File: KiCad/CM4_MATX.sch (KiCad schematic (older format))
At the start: 9 parts

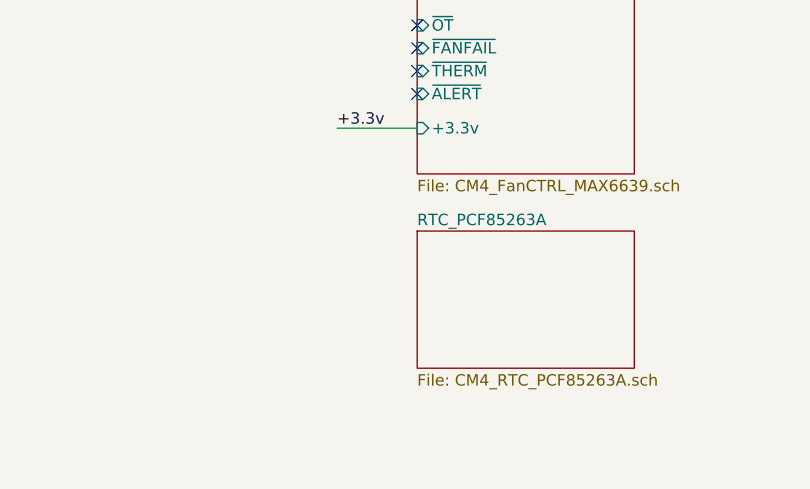
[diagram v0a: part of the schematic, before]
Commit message: updated PCB with RTC circuit
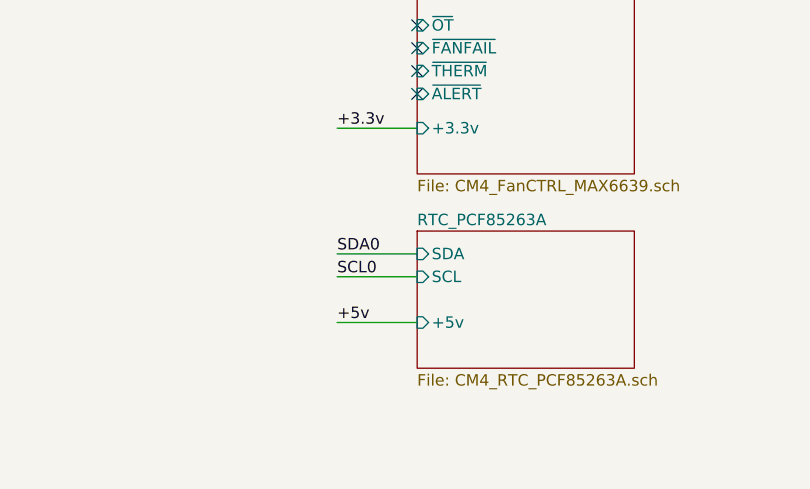
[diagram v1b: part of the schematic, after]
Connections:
- wire segments 78 -> 81
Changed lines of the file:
@@
 F0 "RTC_PCF85263A" 50
 F1 "CM4_RTC_PCF85263A.sch" 50
+F2 "SCL" I L 5400 6850 50
+F3 "SDA" I L 5400 6750 50
+F4 "+5v" I L 5400 7050 50
 $EndSheet
+Wire Wire Line
+	5050 6850 5400 6850
+Text Label 5050 6750 0    50   ~ 0
+SDA0
+Text Label 5050 6850 0    50   ~ 0
+SCL0
+Wire Wire Line
+	5400 6750 5050 6750
+Text Label 5050 7050 0    50   ~ 0
++5v
+Wire Wire Line
+	5400 7050 5050 7050
 $EndSCHEMATC

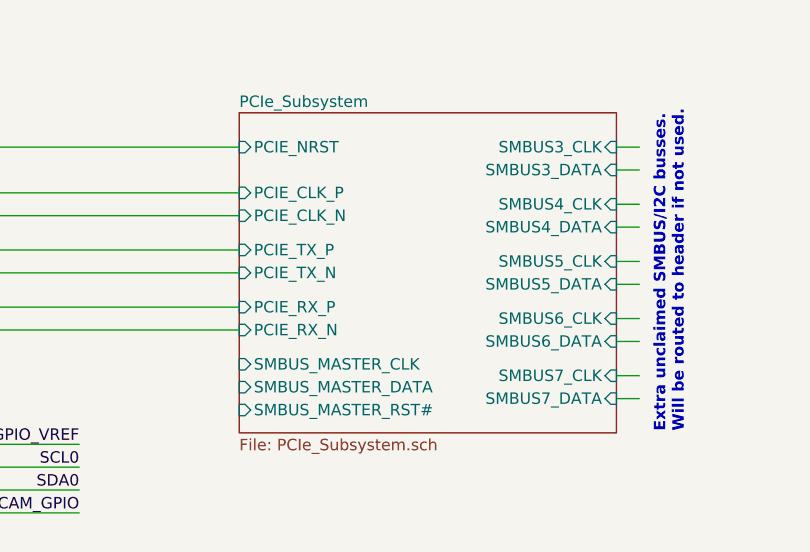
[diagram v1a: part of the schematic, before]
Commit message: Tons of wiring and pin straps for PCI-e Switch
Also re-did some hierarchical labels for JTAG
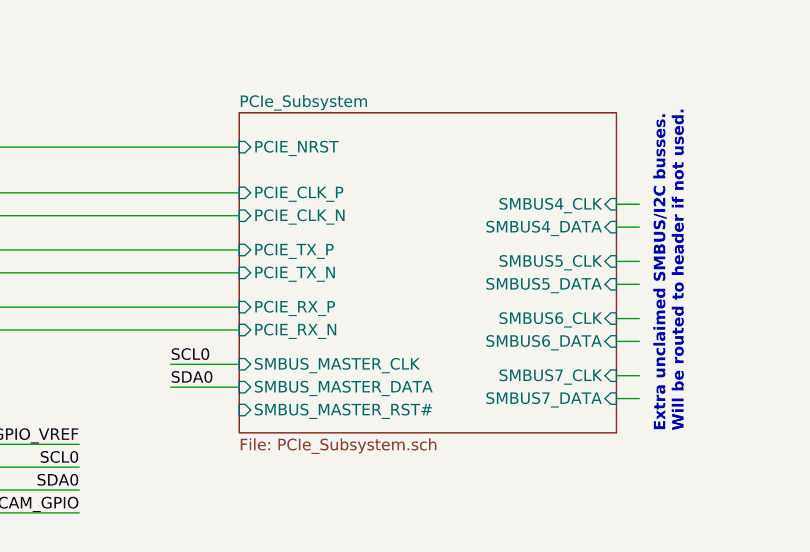
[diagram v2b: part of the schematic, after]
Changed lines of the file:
@@
 F28 "HD2_5v" I L 3050 1100 50
-$EndSheet
-$Sheet
-S 7300 1100 1650 1400
-U 5FFBC089
-F0 "PCIe_Subsystem" 50
-F1 "PCIe_Subsystem.sch" 50
-F2 "PCIE_NRST" I L 7300 1250 50
-F3 "PCIE_CLK_P" I L 7300 1450 50
-F4 "PCIE_CLK_N" I L 7300 1550 50
-F5 "PCIE_TX_P" I L 7300 1700 50
-F6 "PCIE_TX_N" I L 7300 1800 50
-F7 "PCIE_RX_P" I L 7300 1950 50
-F8 "PCIE_RX_N" I L 7300 2050 50
-F9 "SMBUS3_CLK" I R 8950 1250 50
-F10 "SMBUS3_DATA" I R 8950 1350 50
-F11 "SMBUS4_CLK" I R 8950 1500 50
-F12 "SMBUS4_DATA" I R 8950 1600 50
-F13 "SMBUS5_CLK" I R 8950 1750 50
-F14 "SMBUS5_DATA" I R 8950 1850 50
-F15 "SMBUS6_CLK" I R 8950 2000 50
-F16 "SMBUS6_DATA" I R 8950 2100 50
-F17 "SMBUS7_CLK" I R 8950 2250 50
-F18 "SMBUS7_DATA" I R 8950 2350 50
-F19 "SMBUS_MASTER_CLK" I L 7300 2200 50
-F20 "SMBUS_MASTER_DATA" I L 7300 2300 50
-F21 "SMBUS_MASTER_RST#" I L 7300 2400 50
 $EndSheet
 Wire Wire Line
@@
 Wire Wire Line
 	6150 2050 7300 2050
-Wire Wire Line
-	8950 1250 9050 1250
-Wire Wire Line
-	8950 1350 9050 1350
 Wire Wire Line
 	8950 1500 9050 1500
@@
 Wire Wire Line
 	5400 7050 5050 7050
+Text Label 7000 2200 0    50   ~ 0
+SCL0
+Text Label 7000 2300 0    50   ~ 0
+SDA0
+Wire Wire Line
+	7000 2200 7300 2200
+Wire Wire Line
+	7300 2300 7000 2300
+$Sheet
+S 7300 1100 1650 1400
+U 5FFBC089
+F0 "PCIe_Subsystem" 50
+F1 "PCIe_Subsystem.sch" 50
+F2 "PCIE_NRST" I L 7300 1250 50
+F3 "PCIE_CLK_P" I L 7300 1450 50
+F4 "PCIE_CLK_N" I L 7300 1550 50
+F5 "PCIE_TX_P" I L 7300 1700 50
+F6 "PCIE_TX_N" I L 7300 1800 50
+F7 "PCIE_RX_P" I L 7300 1950 50
+F8 "PCIE_RX_N" I L 7300 2050 50
+F9 "SMBUS4_CLK" I R 8950 1500 50
+F10 "SMBUS4_DATA" I R 8950 1600 50
+F11 "SMBUS5_CLK" I R 8950 1750 50
+F12 "SMBUS5_DATA" I R 8950 1850 50
+F13 "SMBUS6_CLK" I R 8950 2000 50
+F14 "SMBUS6_DATA" I R 8950 2100 50
+F15 "SMBUS7_CLK" I R 8950 2250 50
+F16 "SMBUS7_DATA" I R 8950 2350 50
+F17 "SMBUS_MASTER_CLK" I L 7300 2200 50
+F18 "SMBUS_MASTER_DATA" I L 7300 2300 50
+F19 "SMBUS_MASTER_RST#" I L 7300 2400 50
+$EndSheet
 $EndSCHEMATC

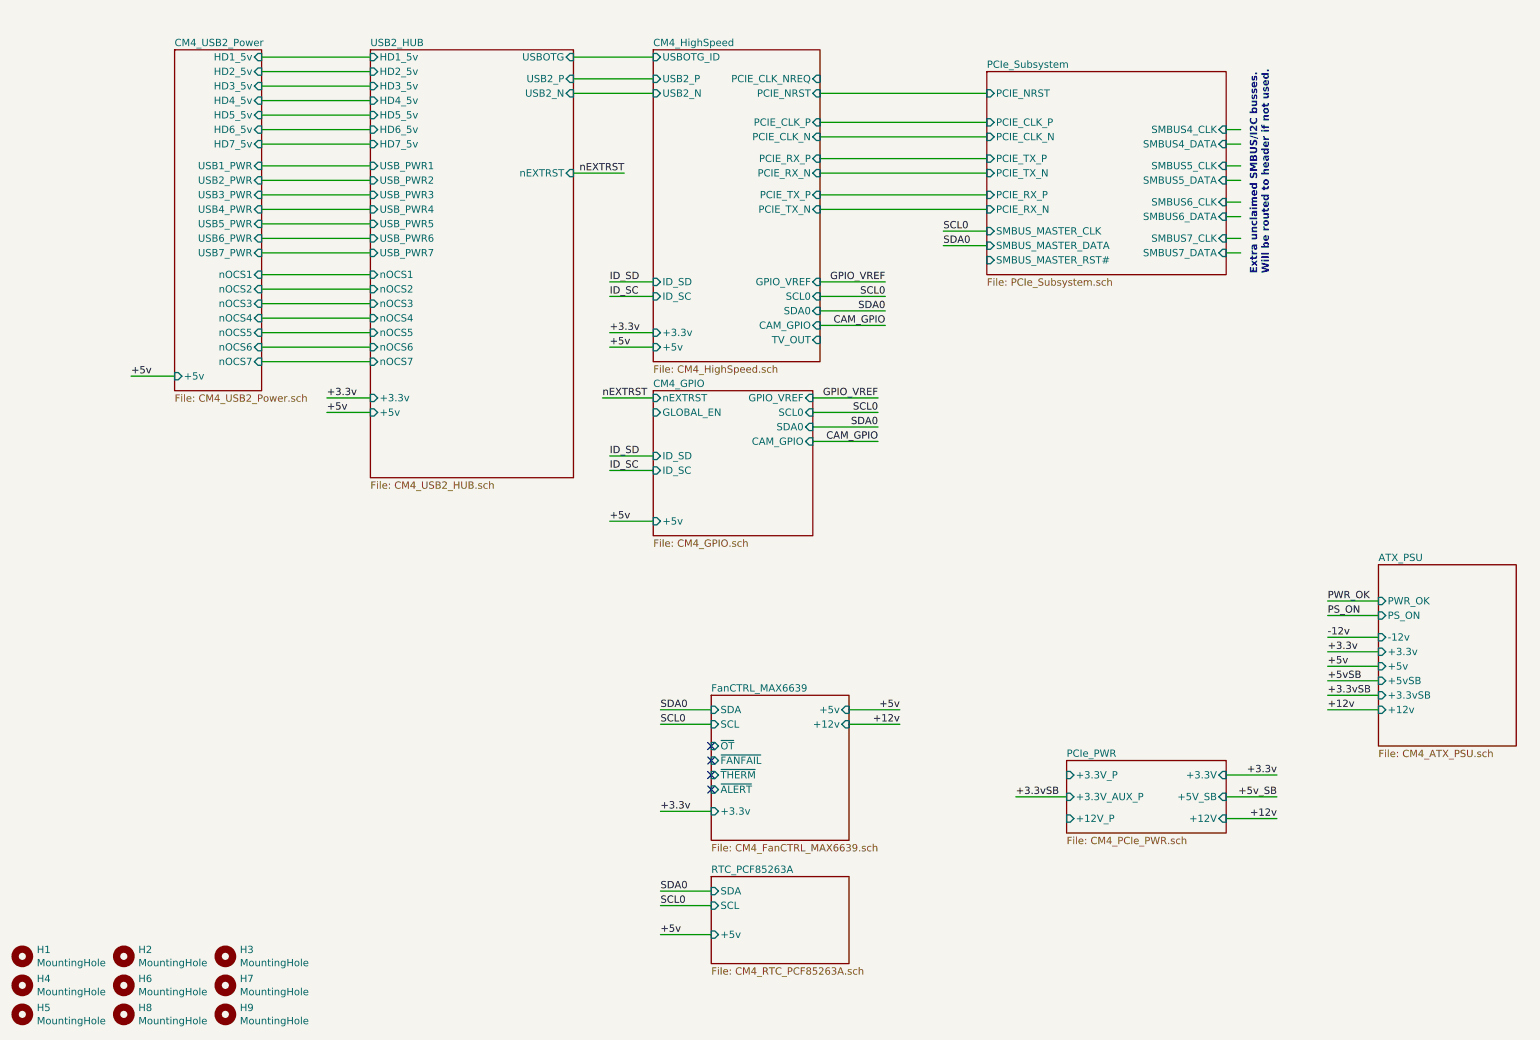
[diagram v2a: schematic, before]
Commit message: PCIe Wiring, resistor value adjustments, and a bunch of small ERC fixes.
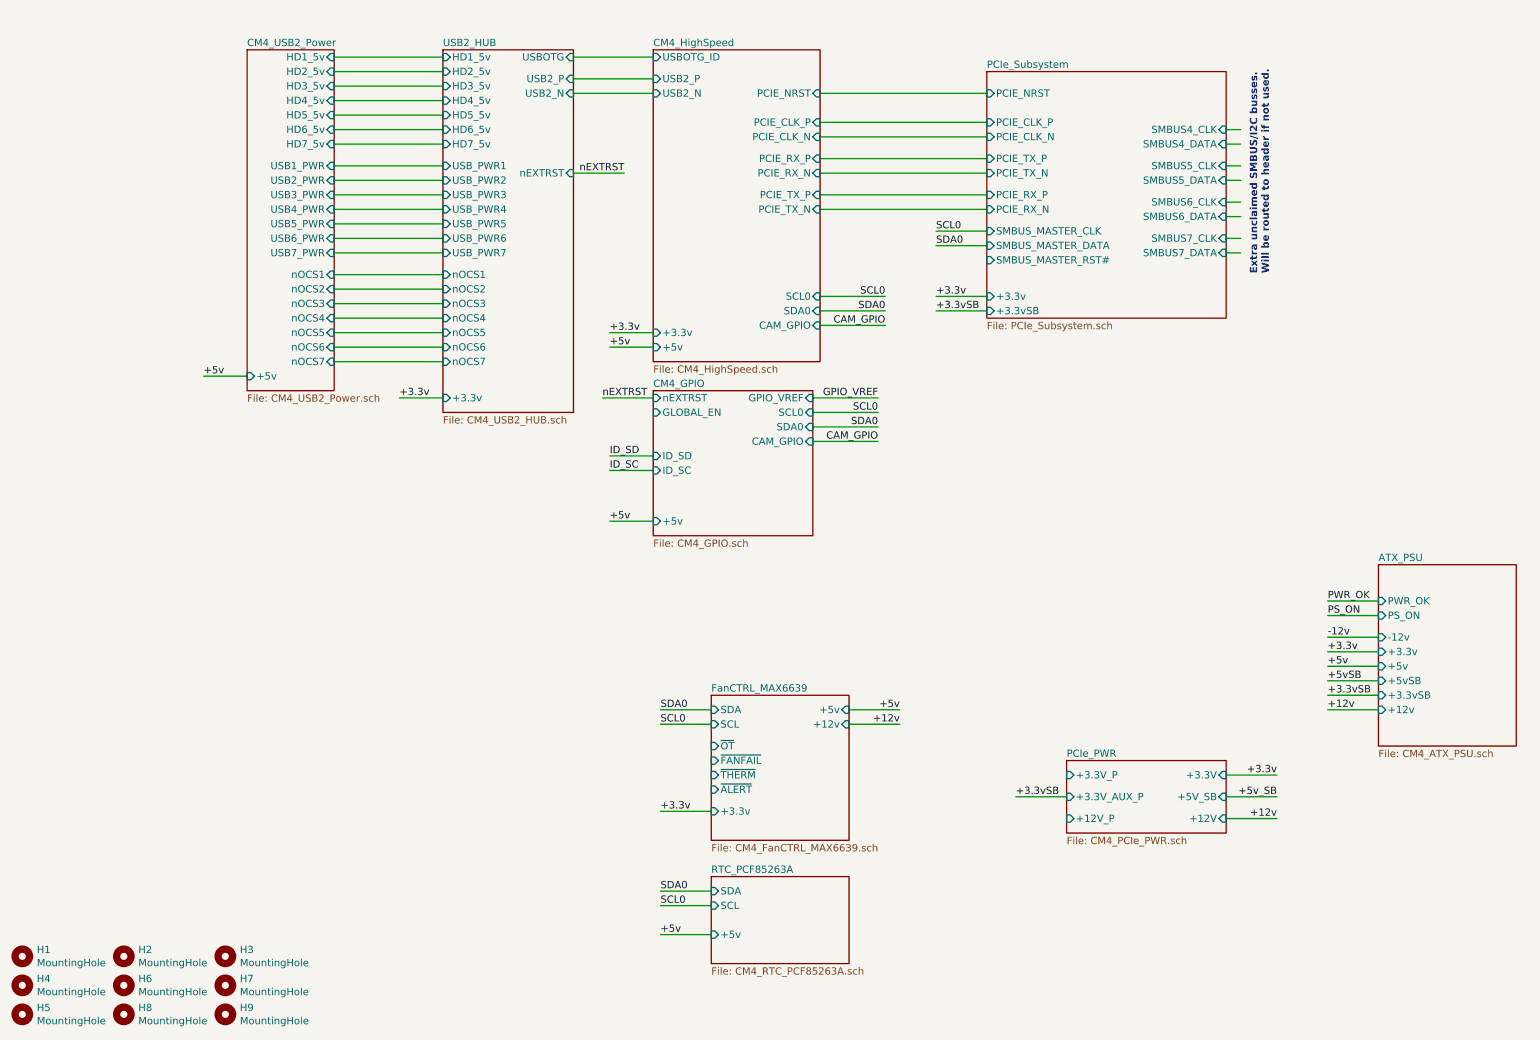
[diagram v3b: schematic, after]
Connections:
- wire segments 81 -> 79
- no-connect marks 4 -> 0
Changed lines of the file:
@@
 F0 "CM4_HighSpeed" 50
 F1 "CM4_HighSpeed.sch" 50
-F2 "TV_OUT" I R 6150 2950 50
-F3 "PCIE_NRST" I R 6150 1250 50
-F4 "USB2_P" I L 5000 1150 50
-F5 "USB2_N" I L 5000 1250 50
-F6 "USBOTG_ID" I L 5000 1000 50
-F7 "CAM_GPIO" I R 6150 2850 50
-F8 "PCIE_CLK_NREQ" I R 6150 1150 50
-F9 "PCIE_CLK_P" I R 6150 1450 50
-F10 "PCIE_CLK_N" I R 6150 1550 50
-F11 "PCIE_RX_P" I R 6150 1700 50
-F12 "PCIE_RX_N" I R 6150 1800 50
-F13 "PCIE_TX_P" I R 6150 1950 50
-F14 "PCIE_TX_N" I R 6150 2050 50
-F15 "+3.3v" I L 5000 2900 50
-F16 "SDA0" I R 6150 2750 50
-F17 "SCL0" I R 6150 2650 50
-F18 "GPIO_VREF" I R 6150 2550 50
-F19 "ID_SC" I L 5000 2650 50
-F20 "ID_SD" I L 5000 2550 50
-F21 "+5v" I L 5000 3000 50
+F2 "PCIE_NRST" I R 6150 1250 50
+F3 "USB2_P" I L 5000 1150 50
+F4 "USB2_N" I L 5000 1250 50
+F5 "USBOTG_ID" I L 5000 1000 50
+F6 "CAM_GPIO" I R 6150 2850 50
+F7 "PCIE_CLK_P" I R 6150 1450 50
+F8 "PCIE_CLK_N" I R 6150 1550 50
+F9 "PCIE_RX_P" I R 6150 1700 50
+F10 "PCIE_RX_N" I R 6150 1800 50
+F11 "PCIE_TX_P" I R 6150 1950 50
+F12 "PCIE_TX_N" I R 6150 2050 50
+F13 "+3.3v" I L 5000 2900 50
+F14 "SDA0" I R 6150 2750 50
+F15 "SCL0" I R 6150 2650 50
+F16 "+5v" I L 5000 3000 50
 $EndSheet
 $Sheet
@@
 +5v
 Wire Wire Line
-	5000 2550 4700 2550
-Text Label 4700 2550 0    50   ~ 0
-ID_SD
-Text Label 4700 2650 0    50   ~ 0
-ID_SC
-Wire Wire Line
-	4700 2650 5000 2650
-Wire Wire Line
 	5000 3750 4700 3750
 Text Label 4700 3750 0    50   ~ 0
@@
 	4450 1000 5000 1000
 Text Label 6550 3350 2    50   ~ 0
-GPIO_VREF
-Text Label 6600 2550 2    50   ~ 0
 GPIO_VREF
 Text Label 6600 2650 2    50   ~ 0
@@
 Wire Wire Line
 	6600 2650 6150 2650
-Wire Wire Line
-	6150 2550 6600 2550
 $Sheet
 S 5000 3300 1100 1000
@@
 Wire Wire Line
 	5400 5500 5050 5500
-NoConn ~ 5400 5750
-NoConn ~ 5400 5850
-NoConn ~ 5400 5950
-NoConn ~ 5400 6050
 Text Label 9650 5400 0    50   ~ 0
 +3.3vSB
@@
 	7500 6100 7850 6100
 Wire Wire Line
-	2300 1850 3050 1850
-Wire Wire Line
-	2300 1950 3050 1950
-Wire Wire Line
-	2300 2050 3050 2050
-Wire Wire Line
-	2300 2150 3050 2150
-Wire Wire Line
-	2300 2250 3050 2250
-Wire Wire Line
-	2300 2350 3050 2350
-Wire Wire Line
-	2300 1750 3050 1750
-Wire Wire Line
-	2300 1600 3050 1600
-Wire Wire Line
-	2300 1500 3050 1500
-Wire Wire Line
-	2300 1400 3050 1400
-Wire Wire Line
-	2300 1300 3050 1300
-Wire Wire Line
-	2300 1200 3050 1200
-Wire Wire Line
-	2300 1100 3050 1100
-Wire Wire Line
-	2300 1000 3050 1000
-Wire Wire Line
-	2300 2500 3050 2500
-Wire Wire Line
-	2300 2600 3050 2600
-Wire Wire Line
-	2300 2700 3050 2700
-Wire Wire Line
-	2300 2800 3050 2800
-Wire Wire Line
-	2300 2900 3050 2900
-Wire Wire Line
-	2300 3000 3050 3000
-Wire Wire Line
-	2300 3100 3050 3100
-$Sheet
-S 1700 950  600  2350
+	2800 1850 3550 1850
+Wire Wire Line
+	2800 1950 3550 1950
+Wire Wire Line
+	2800 2050 3550 2050
+Wire Wire Line
+	2800 2150 3550 2150
+Wire Wire Line
+	2800 2250 3550 2250
+Wire Wire Line
+	2800 2350 3550 2350
+Wire Wire Line
+	2800 1750 3550 1750
+Wire Wire Line
+	2800 1600 3550 1600
+Wire Wire Line
+	2800 1500 3550 1500
+Wire Wire Line
+	2800 1400 3550 1400
+Wire Wire Line
+	2800 1300 3550 1300
+Wire Wire Line
+	2800 1200 3550 1200
+Wire Wire Line
+	2800 1100 3550 1100
+Wire Wire Line
+	2800 1000 3550 1000
+Wire Wire Line
+	2800 2500 3550 2500
+Wire Wire Line
+	2800 2600 3550 2600
+Wire Wire Line
+	2800 2700 3550 2700
+Wire Wire Line
+	2800 2800 3550 2800
+Wire Wire Line
+	2800 2900 3550 2900
+Wire Wire Line
+	2800 3000 3550 3000
+Wire Wire Line
+	2800 3100 3550 3100
+$Sheet
+S 2200 950  600  2350
 U 608D2490
 F0 "CM4_USB2_Power" 50
 F1 "CM4_USB2_Power.sch" 50
-F2 "+5v" I L 1700 3200 50
-F3 "USB1_PWR" I R 2300 1750 50
-F4 "nOCS1" I R 2300 2500 50
-F5 "HD1_5v" I R 2300 1000 50
-F6 "USB2_PWR" I R 2300 1850 50
-F7 "nOCS2" I R 2300 2600 50
-F8 "HD2_5v" I R 2300 1100 50
-F9 "USB3_PWR" I R 2300 1950 50
-F10 "nOCS3" I R 2300 2700 50
-F11 "HD3_5v" I R 2300 1200 50
-F12 "USB4_PWR" I R 2300 2050 50
-F13 "HD4_5v" I R 2300 1300 50
-F14 "nOCS4" I R 2300 2800 50
-F15 "USB5_PWR" I R 2300 2150 50
-F16 "nOCS5" I R 2300 2900 50
-F17 "HD5_5v" I R 2300 1400 50
-F18 "USB6_PWR" I R 2300 2250 50
-F19 "nOCS6" I R 2300 3000 50
-F20 "HD6_5v" I R 2300 1500 50
-F21 "USB7_PWR" I R 2300 2350 50
-F22 "nOCS7" I R 2300 3100 50
-F23 "HD7_5v" I R 2300 1600 50
-$EndSheet
-Text Label 1400 3200 0    50   ~ 0
+F2 "+5v" I L 2200 3200 50
+F3 "USB1_PWR" I R 2800 1750 50
+F4 "nOCS1" I R 2800 2500 50
+F5 "HD1_5v" I R 2800 1000 50
+F6 "USB2_PWR" I R 2800 1850 50
+F7 "nOCS2" I R 2800 2600 50
+F8 "HD2_5v" I R 2800 1100 50
+F9 "USB3_PWR" I R 2800 1950 50
+F10 "nOCS3" I R 2800 2700 50
+F11 "HD3_5v" I R 2800 1200 50
+F12 "USB4_PWR" I R 2800 2050 50
+F13 "HD4_5v" I R 2800 1300 50
+F14 "nOCS4" I R 2800 2800 50
+F15 "USB5_PWR" I R 2800 2150 50
+F16 "nOCS5" I R 2800 2900 50
+F17 "HD5_5v" I R 2800 1400 50
+F18 "USB6_PWR" I R 2800 2250 50
+F19 "nOCS6" I R 2800 3000 50
+F20 "HD6_5v" I R 2800 1500 50
+F21 "USB7_PWR" I R 2800 2350 50
+F22 "nOCS7" I R 2800 3100 50
+F23 "HD7_5v" I R 2800 1600 50
+$EndSheet
+Text Label 1900 3200 0    50   ~ 0
 +5v
 Wire Wire Line
-	1700 3200 1400 3200
-Wire Wire Line
-	2750 3350 3050 3350
-Wire Wire Line
-	3050 3450 2750 3450
-Text Label 2750 3350 0    50   ~ 0
+	2200 3200 1900 3200
+Wire Wire Line
+	3250 3350 3550 3350
+Text Label 3250 3350 0    50   ~ 0
 +3.3v
-Text Label 2750 3450 0    50   ~ 0
-+5v
-$Sheet
-S 3050 950  1400 2950
+$Sheet
+S 3550 950  900  2500
 U 5FB43DAF
 F0 "USB2_HUB" 50
@@
 F4 "USB2_P" I R 4450 1150 50
 F5 "USB2_N" I R 4450 1250 50
-F6 "+5v" I L 3050 3450 50
-F7 "+3.3v" I L 3050 3350 50
-F8 "nOCS5" I L 3050 2900 50
-F9 "nOCS7" I L 3050 3100 50
-F10 "nOCS6" I L 3050 3000 50
-F11 "USB_PWR6" I L 3050 2250 50
-F12 "USB_PWR7" I L 3050 2350 50
-F13 "USB_PWR4" I L 3050 2050 50
-F14 "nOCS4" I L 3050 2800 50
-F15 "nOCS3" I L 3050 2700 50
-F16 "USB_PWR3" I L 3050 1950 50
-F17 "USB_PWR2" I L 3050 1850 50
-F18 "nOCS2" I L 3050 2600 50
-F19 "nOCS1" I L 3050 2500 50
-F20 "USB_PWR1" I L 3050 1750 50
-F21 "USB_PWR5" I L 3050 2150 50
-F22 "HD1_5v" I L 3050 1000 50
-F23 "HD7_5v" I L 3050 1600 50
-F24 "HD3_5v" I L 3050 1200 50
-F25 "HD4_5v" I L 3050 1300 50
-F26 "HD5_5v" I L 3050 1400 50
-F27 "HD6_5v" I L 3050 1500 50
-F28 "HD2_5v" I L 3050 1100 50
+F6 "+3.3v" I L 3550 3350 50
+F7 "nOCS5" I L 3550 2900 50
+F8 "nOCS7" I L 3550 3100 50
+F9 "nOCS6" I L 3550 3000 50
+F10 "USB_PWR6" I L 3550 2250 50
+F11 "USB_PWR7" I L 3550 2350 50
+F12 "USB_PWR4" I L 3550 2050 50
+F13 "nOCS4" I L 3550 2800 50
+F14 "nOCS3" I L 3550 2700 50
+F15 "USB_PWR3" I L 3550 1950 50
+F16 "USB_PWR2" I L 3550 1850 50
+F17 "nOCS2" I L 3550 2600 50
+F18 "nOCS1" I L 3550 2500 50
+F19 "USB_PWR1" I L 3550 1750 50
+F20 "USB_PWR5" I L 3550 2150 50
+F21 "HD1_5v" I L 3550 1000 50
+F22 "HD7_5v" I L 3550 1600 50
+F23 "HD3_5v" I L 3550 1200 50
+F24 "HD4_5v" I L 3550 1300 50
+F25 "HD5_5v" I L 3550 1400 50
+F26 "HD6_5v" I L 3550 1500 50
+F27 "HD2_5v" I L 3550 1100 50
 $EndSheet
 Wire Wire Line
@@
 Wire Wire Line
 	5400 7050 5050 7050
-Text Label 7000 2200 0    50   ~ 0
+Text Label 6950 2200 0    50   ~ 0
 SCL0
-Text Label 7000 2300 0    50   ~ 0
+Text Label 6950 2300 0    50   ~ 0
 SDA0
-Wire Wire Line
-	7000 2200 7300 2200
-Wire Wire Line
-	7300 2300 7000 2300
-$Sheet
-S 7300 1100 1650 1400
+$Sheet
+S 7300 1100 1650 1700
 U 5FFBC089
 F0 "PCIe_Subsystem" 50
@@
 F18 "SMBUS_MASTER_DATA" I L 7300 2300 50
 F19 "SMBUS_MASTER_RST#" I L 7300 2400 50
-$EndSheet
+F20 "+3.3v" I L 7300 2650 50
+F21 "+3.3vSB" I L 7300 2750 50
+$EndSheet
+Text Label 6950 2650 0    50   ~ 0
++3.3v
+Text Label 6950 2750 0    50   ~ 0
++3.3vSB
+Wire Wire Line
+	6950 2650 7300 2650
+Wire Wire Line
+	6950 2750 7300 2750
+Wire Wire Line
+	6950 2200 7300 2200
+Wire Wire Line
+	6950 2300 7300 2300
 $EndSCHEMATC
